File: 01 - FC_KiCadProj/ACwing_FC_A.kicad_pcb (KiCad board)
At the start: 4 copper layers, 40.8 x 40.8 mm, 111 parts, among them J1 USB-C (HRO TYPE-C-31-M-12), J2 ESC link, J3 Qwiic, J4 Qwiic, J5 ELRS, J6 ESC link B, J7 VBAT+, J8 GND, Q5 AO3401A, U1 LSM6DSV16X, U10 W25Q128JV, U11 LDK130PU-R, U12 LM5166DRCT, U13 SN74LV1T34DCKR, U2 STM32WB55CGU6, U3 IIS2MDC, U4 LPS22HH, U5 LD39130SPUR, U7 USBLC6-2SC6, U8 MLPF-WB55-01E3, Y1 32MHz

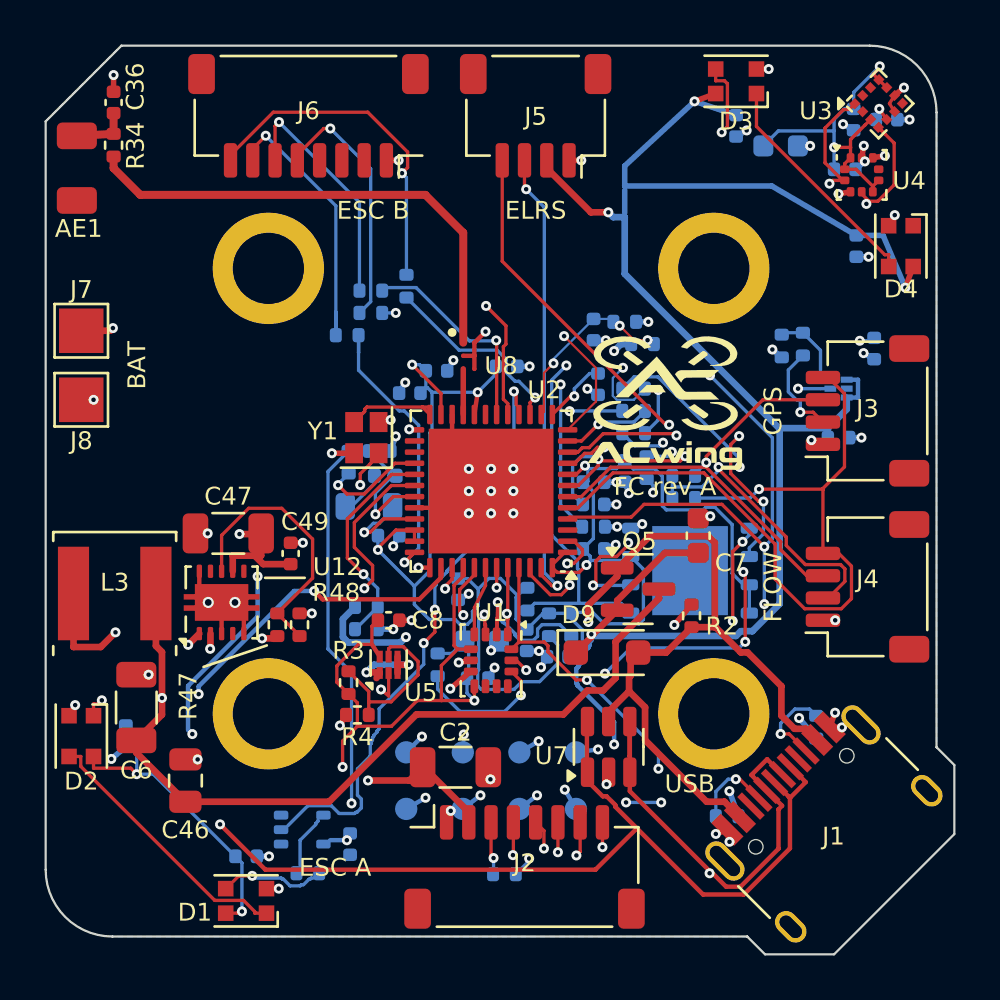
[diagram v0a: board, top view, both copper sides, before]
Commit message: Removed references of the passive components and of the ICs on the top and bottom silkscreen. Left only the labels of the connectors.
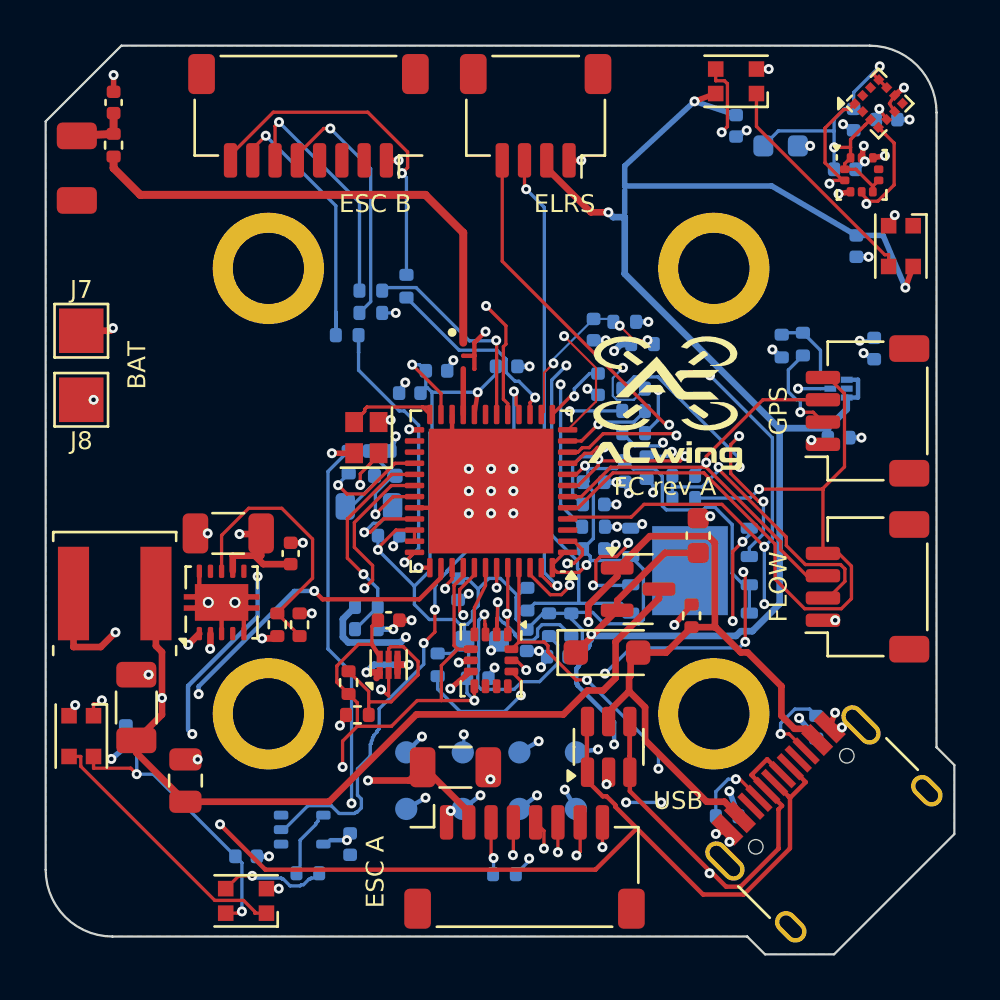
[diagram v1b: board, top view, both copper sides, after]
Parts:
- moved LOGO2 2.89 mm to (136.0, 99.5)
